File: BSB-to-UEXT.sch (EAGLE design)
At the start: 22 parts, among them Q1 BC847, Q2 BC857

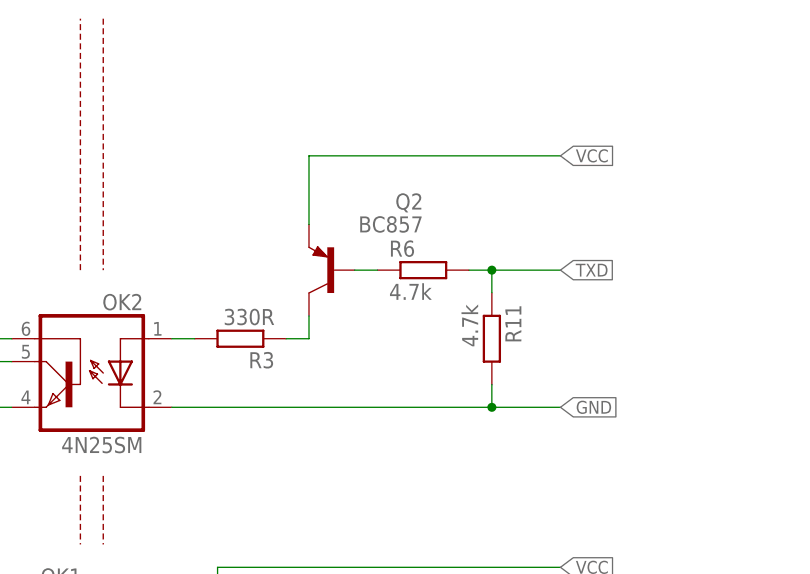
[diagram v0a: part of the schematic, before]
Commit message: Change BSB-to-UEXT Tx Pin Assignment
Follow the BSB-LAN repo in moving TX onto the UEXT-SSEL pin instead of the UEXT-TX pin. This is done to avoid issues with the TX pin needing to be pulled low during the boot phase, but that in turn would "short" out the BSB bus until everything is booted up.
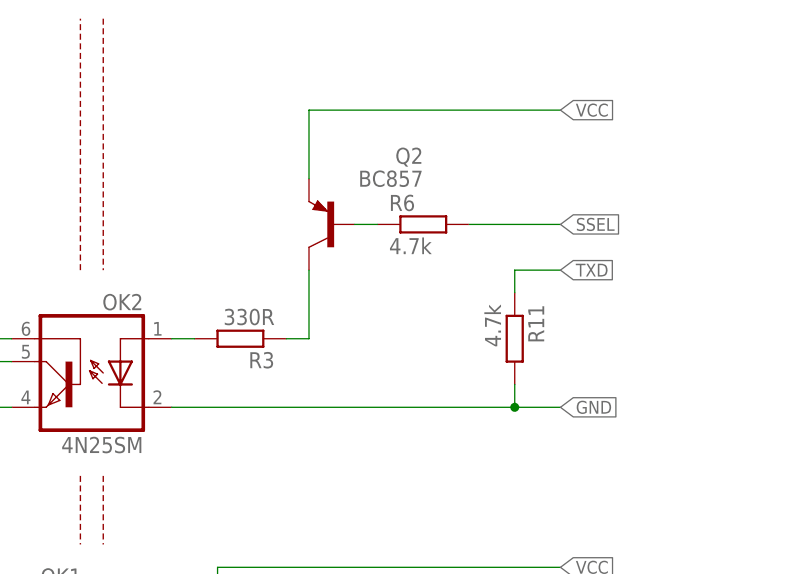
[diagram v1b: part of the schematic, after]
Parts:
- R11: device BSB-LAN:R-EU_R0805L -> BSB-LAN:R-EU_R0805
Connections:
- net SSEL: now also R6.2
- net TXD: no longer R6.2
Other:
- moved on the sheet: Q2, R11, R6
